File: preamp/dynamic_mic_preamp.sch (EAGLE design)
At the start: 12 parts

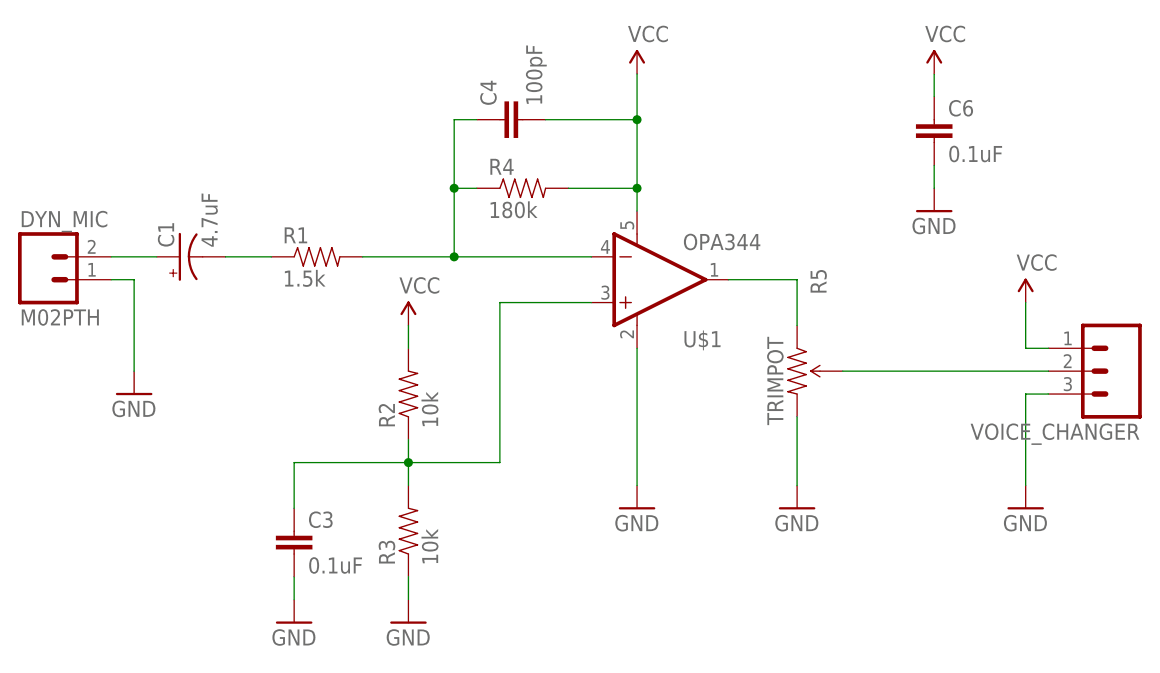
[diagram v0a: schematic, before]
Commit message: started work on single board version
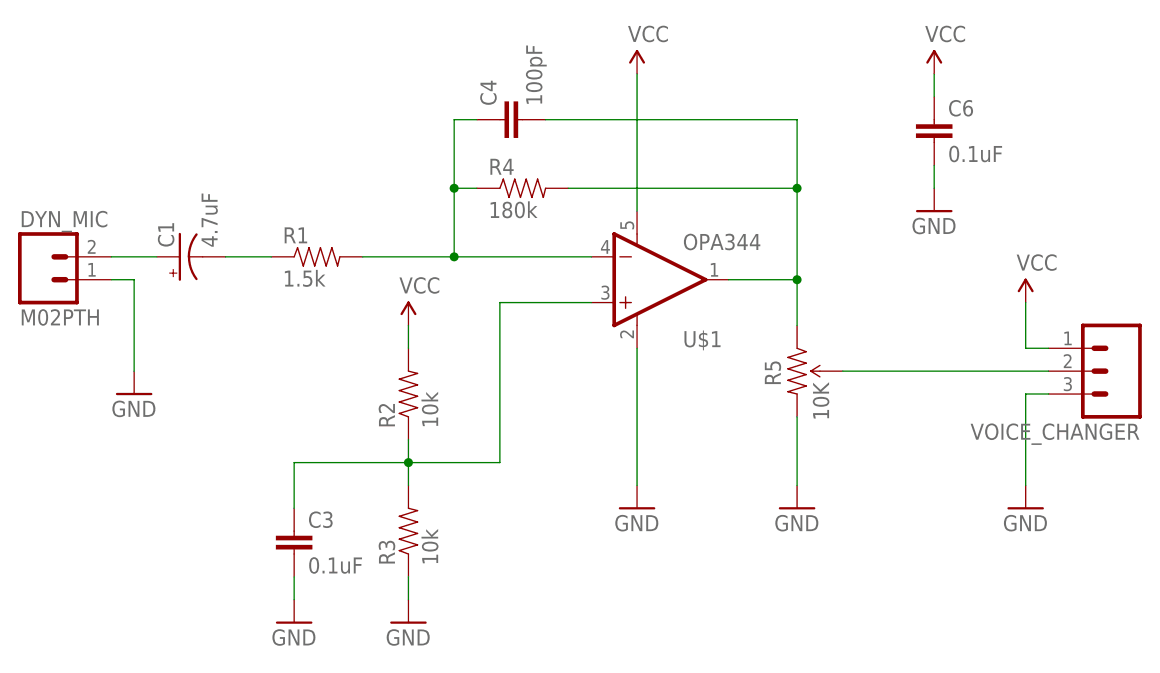
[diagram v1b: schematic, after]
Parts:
- R5: value TRIMPOT -> 10K
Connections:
- net N$4: now also C4.2, R4.2
- net VCC: no longer C4.2, R4.2
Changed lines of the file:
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@@
 <part name="DYN_MIC" library="SparkFun-Connectors" deviceset="M02" device="PTH"/>
 <part name="GND7" library="SparkFun-Aesthetics" deviceset="GND" device=""/>
-<part name="R5" library="SparkFun-Electromechanical" deviceset="TRIMPOT" device=""/>
+<part name="R5" library="SparkFun-Electromechanical" deviceset="TRIMPOT" device="" value="10K"/>
 <part name="VOICE_CHANGER" library="SparkFun-Connectors" deviceset="M03" device="PTH"/>
 <part name="SUPPLY4" library="SparkFun-Aesthetics" deviceset="VCC" device=""/>
@@
 <instance part="DYN_MIC" gate="G$1" x="-7.62" y="71.12"/>
 <instance part="GND7" gate="1" x="2.54" y="58.42"/>
-<instance part="R5" gate="R?" x="76.2" y="60.96" rot="R270"/>
+<instance part="R5" gate="R?" x="76.2" y="60.96" smashed="yes" rot="R270">
+<attribute name="NAME" x="72.6186" y="62.23" size="1.778" layer="95" rot="R270"/>
+<attribute name="VALUE" x="77.978" y="59.69" size="1.778" layer="96" rot="R270"/>
+</instance>
 <instance part="VOICE_CHANGER" gate="G$1" x="111.76" y="60.96" rot="R180"/>
 <instance part="SUPPLY4" gate="G$1" x="101.6" y="68.58"/>
@@
 <pinref part="SUPPLY2" gate="G$1" pin="VCC"/>
 <pinref part="U$1" gate="G$1" pin="V+"/>
-<wire x1="58.42" y1="93.98" x2="58.42" y2="88.9" width="0.1524" layer="91"/>
-<pinref part="R4" gate="G$1" pin="2"/>
-<wire x1="58.42" y1="88.9" x2="58.42" y2="81.28" width="0.1524" layer="91"/>
-<wire x1="58.42" y1="81.28" x2="58.42" y2="78.74" width="0.1524" layer="91"/>
-<wire x1="50.8" y1="81.28" x2="58.42" y2="81.28" width="0.1524" layer="91"/>
-<pinref part="C4" gate="G$1" pin="2"/>
-<wire x1="48.26" y1="88.9" x2="58.42" y2="88.9" width="0.1524" layer="91"/>
-<junction x="58.42" y="81.28"/>
-<junction x="58.42" y="88.9"/>
+<wire x1="58.42" y1="93.98" x2="58.42" y2="78.74" width="0.1524" layer="91"/>
 </segment>
 <segment>
@@
 <wire x1="68.58" y1="71.12" x2="76.2" y2="71.12" width="0.1524" layer="91"/>
 <wire x1="76.2" y1="71.12" x2="76.2" y2="66.04" width="0.1524" layer="91"/>
+<junction x="76.2" y="71.12"/>
+<wire x1="76.2" y1="71.12" x2="76.2" y2="81.28" width="0.1524" layer="91"/>
+<pinref part="R4" gate="G$1" pin="2"/>
+<wire x1="76.2" y1="81.28" x2="50.8" y2="81.28" width="0.1524" layer="91"/>
+<junction x="76.2" y="81.28"/>
+<wire x1="76.2" y1="81.28" x2="76.2" y2="88.9" width="0.1524" layer="91"/>
+<pinref part="C4" gate="G$1" pin="2"/>
+<wire x1="76.2" y1="88.9" x2="48.26" y2="88.9" width="0.1524" layer="91"/>
 </segment>
 </net>
